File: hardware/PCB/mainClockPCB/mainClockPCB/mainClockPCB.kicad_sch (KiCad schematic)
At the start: 61 parts, among them IC1 TMP275AIDR, IC2 SPX1117M3-L_TR, IC3 MCP7940N-I_P, IC4 PAM8904QJER, J1 USB_C_Receptacle_USB2.0_16P, J2 Conn_01x09_Socket, J3 Conn_01x02_Socket, J4 Conn_01x08, J5 Conn_01x09, J6 Conn_01x09, J7 Conn_01x05, J8 Conn_01x06, J9 Conn_01x05, SW1 SW_Push, SW2 SW_Push, U1 PEC11R-4320K-S0012, U2 USBLC6-2SC6, U3 ESP32-S3-WROOM-2, U4 74HC165, Y1 AB26T-32.768KHZ-6

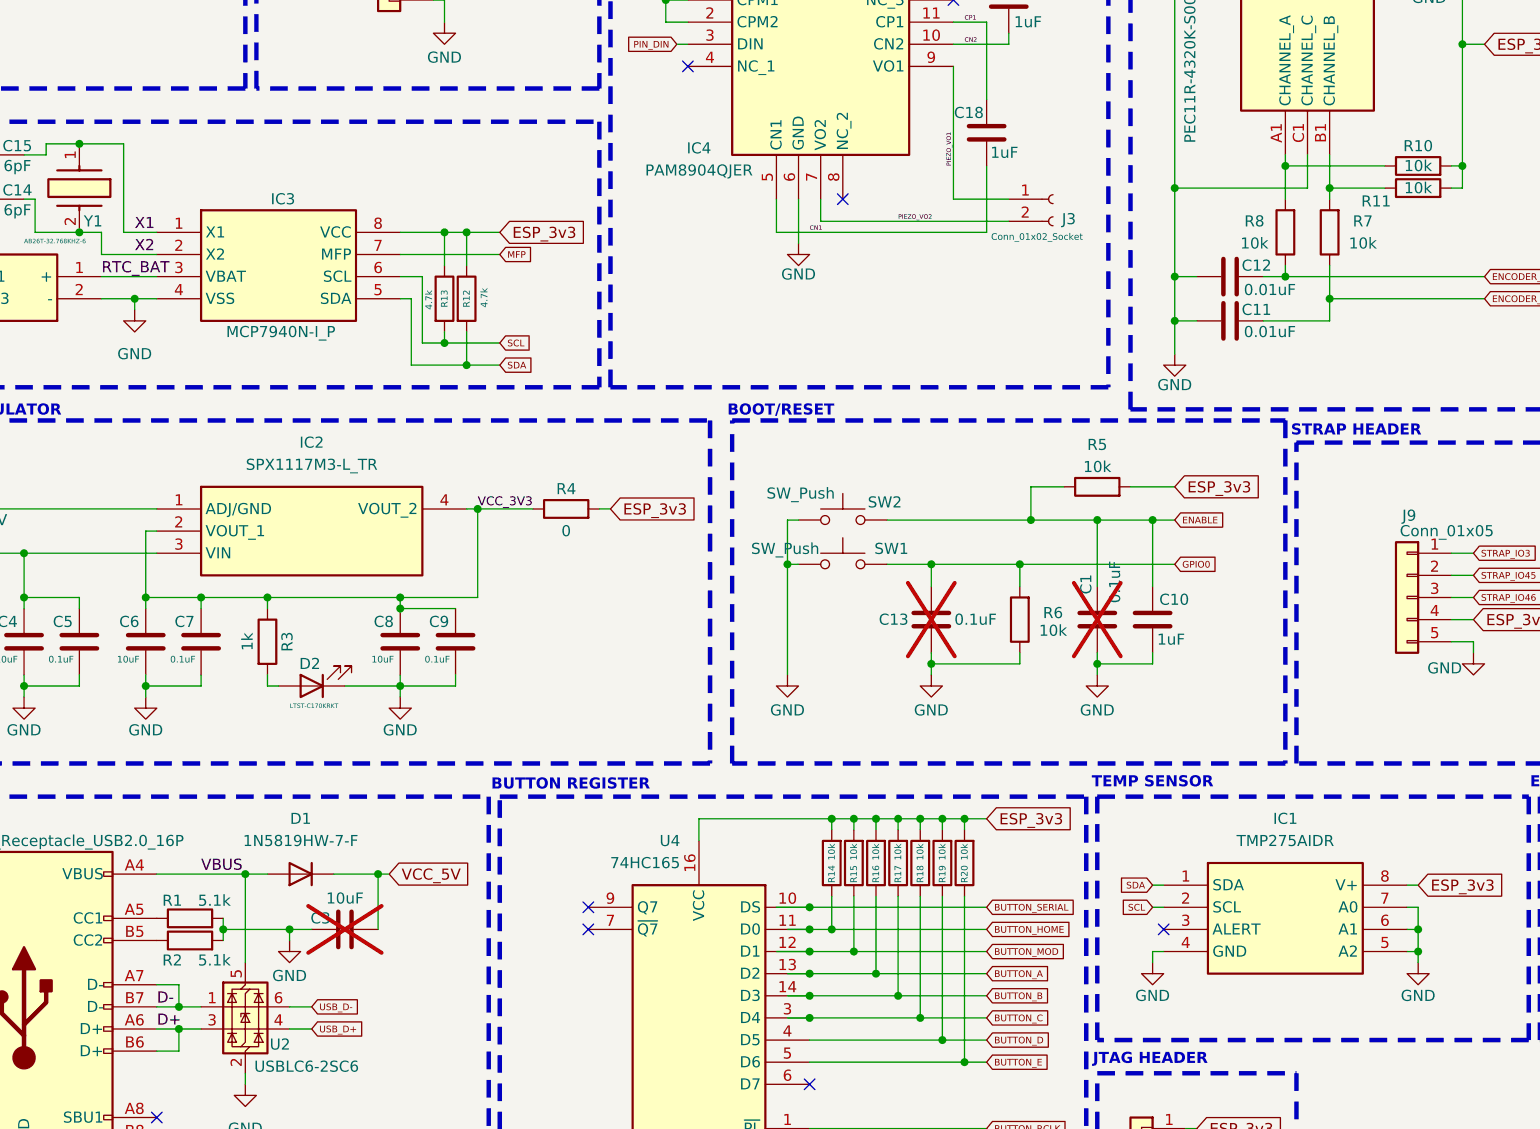
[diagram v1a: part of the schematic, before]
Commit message: net label fixes
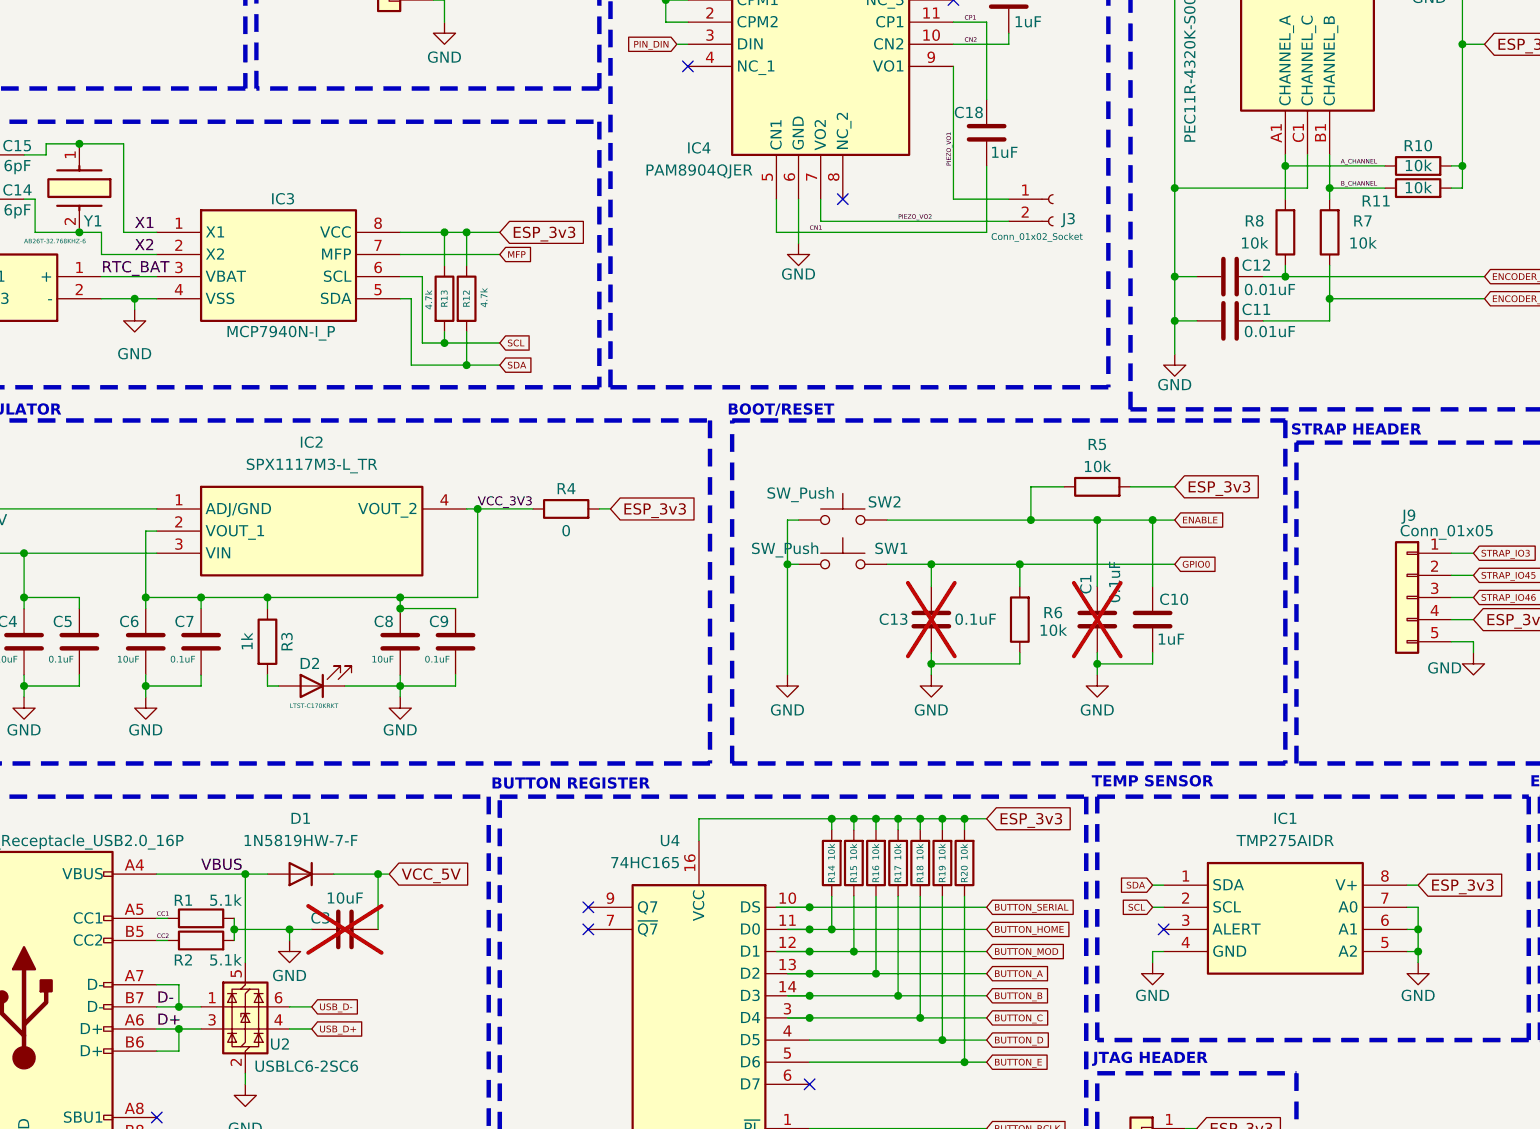
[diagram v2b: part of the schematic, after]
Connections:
- net B_CHANNEL: now reaches R11.1, R7.2, U1.B1 (CHANNEL_B)
- net A_CHANNEL: now reaches R10.1, R8.2, U1.A1 (CHANNEL_A)
- net CC1: now reaches J1.A5 (CC1), R1.1
- net CC2: now reaches J1.B5 (CC2), R2.1
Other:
- moved on the sheet: R1, R2
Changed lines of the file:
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@@
 	)
 	(junction
-		(at 52.07 151.13)
+		(at 53.34 151.13)
 		(diameter 0)
 		(color 0 0 0 0)
@@
 	(wire
 		(pts
-			(xy 52.07 149.86) (xy 52.07 151.13)
+			(xy 53.34 149.86) (xy 53.34 151.13)
 		)
 		(stroke
@@
 	(wire
 		(pts
-			(xy 52.07 151.13) (xy 52.07 152.4)
+			(xy 53.34 151.13) (xy 53.34 152.4)
 		)
 		(stroke
@@
 	(wire
 		(pts
+			(xy 45.72 149.86) (xy 44.45 149.86)
+		)
+		(stroke
+			(width 0)
+			(type default)
+		)
+	)
+	(wire
+		(pts
 			(xy 54.61 144.78) (xy 57.15 144.78)
 		)
@@
 	(wire
 		(pts
-			(xy 52.07 151.13) (xy 59.69 151.13)
+			(xy 53.34 151.13) (xy 59.69 151.13)
 		)
 		(stroke
@@
 	(wire
 		(pts
+			(xy 45.72 152.4) (xy 44.45 152.4)
+		)
+		(stroke
+			(width 0)
+			(type default)
+		)
+	)
+	(wire
+		(pts
 			(xy 134.62 138.43) (xy 134.62 139.7)
 		)
@@
 		)
 	)
+	(label "B_CHANNEL"
+		(at 180.34 66.04 0)
+		(effects
+			(font
+				(size 0.508 0.508)
+			)
+			(justify left bottom)
+		)
+	)
 	(label "X2"
 		(at 41.91 73.66 0)
@@
 		)
 	)
+	(label "A_CHANNEL"
+		(at 180.34 63.5 0)
+		(effects
+			(font
+				(size 0.508 0.508)
+			)
+			(justify left bottom)
+		)
+	)
 	(label "CP1"
 		(at 137.16 46.99 0)
@@
 		)
 	)
+	(label "CC1"
+		(at 44.45 149.86 0)
+		(effects
+			(font
+				(size 0.508 0.508)
+			)
+			(justify left bottom)
+		)
+	)
 	(label "D-"
 		(at 44.45 160.02 0)
@@
 		)
 	)
+	(label "CC2"
+		(at 44.45 152.4 0)
+		(effects
+			(font
+				(size 0.508 0.508)
+			)
+			(justify left bottom)
+		)
+	)
 	(label "VBUS"
 		(at 49.53 144.78 0)
@@
 	(symbol
 		(lib_id "Device:R")
-		(at 48.26 149.86 90)
+		(at 49.53 149.86 90)
 		(unit 1)
 		(exclude_from_sim no)
@@
 		(dnp no)
 		(property "Reference" "R1"
-			(at 46.228 147.828 90)
+			(at 47.498 147.828 90)
 			(effects
 				(font
@@
 		)
 		(property "Value" "5.1k"
-			(at 51.054 147.828 90)
+			(at 52.324 147.828 90)
 			(effects
 				(font
@@
 		)
 		(property "Footprint" "Resistor_SMD:R_0603_1608Metric_Pad0.98x0.95mm_HandSolder"
-			(at 48.26 151.638 90)
+			(at 49.53 151.638 90)
 			(effects
 				(font
@@
 		)
 		(property "Datasheet" "~"
-			(at 48.26 149.86 0)
+			(at 49.53 149.86 0)
 			(effects
 				(font
@@
 		)
 		(property "Description" "Resistor"
-			(at 48.26 149.86 0)
+			(at 49.53 149.86 0)
 			(effects
 				(font
@@
 	(symbol
 		(lib_id "Device:R")
-		(at 48.26 152.4 90)
+		(at 49.53 152.4 90)
 		(unit 1)
 		(exclude_from_sim no)
@@
 		(dnp no)
 		(property "Reference" "R2"
-			(at 46.228 154.686 90)
+			(at 47.498 154.686 90)
 			(effects
 				(font
@@
 		)
 		(property "Value" "5.1k"
-			(at 51.054 154.686 90)
+			(at 52.324 154.686 90)
 			(effects
 				(font
@@
 		)
 		(property "Footprint" "Resistor_SMD:R_0603_1608Metric_Pad0.98x0.95mm_HandSolder"
-			(at 48.26 154.178 90)
+			(at 49.53 154.178 90)
 			(effects
 				(font
@@
 		)
 		(property "Datasheet" "~"
-			(at 48.26 152.4 0)
+			(at 49.53 152.4 0)
 			(effects
 				(font
@@
 		)
 		(property "Description" "Resistor"
-			(at 48.26 152.4 0)
+			(at 49.53 152.4 0)
 			(effects
 				(font

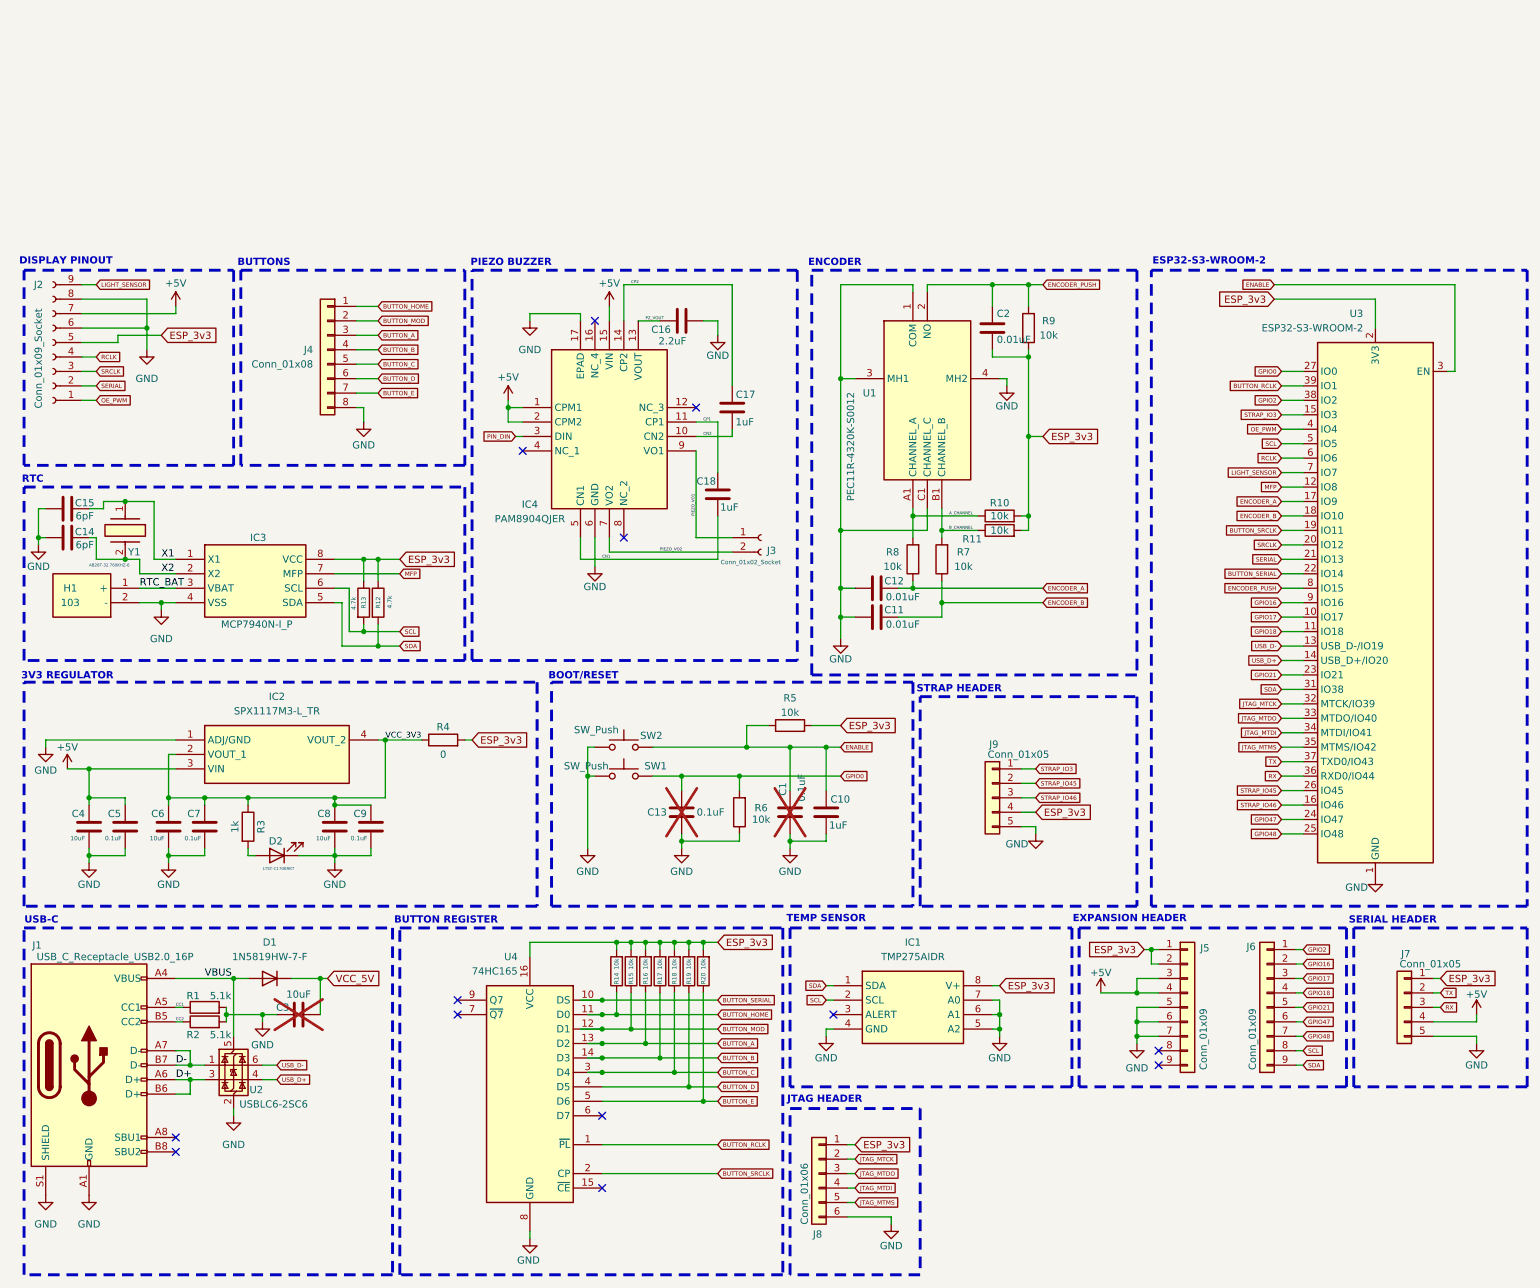
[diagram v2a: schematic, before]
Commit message: power flags
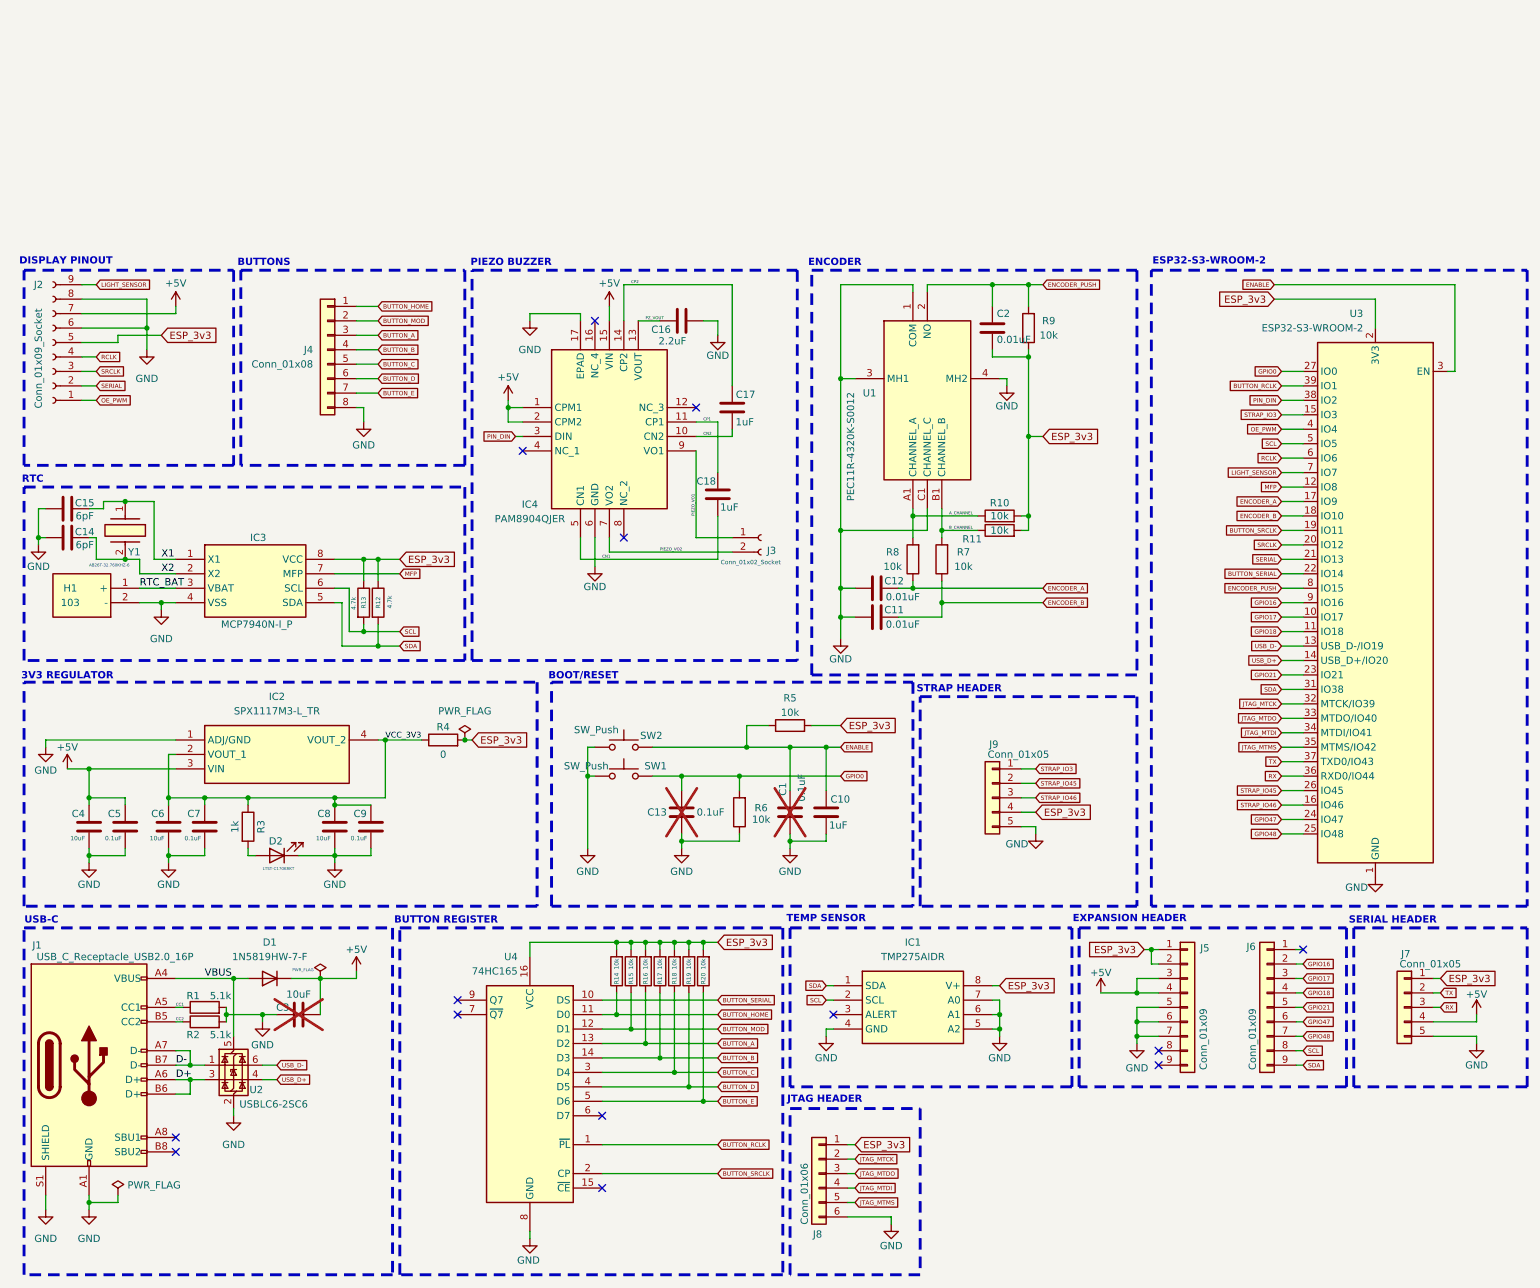
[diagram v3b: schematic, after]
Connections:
- net VCC_5V is gone; now on net +5V: C3.2, D1.1 (K)
- net PIN_DIN: now also U3.38 (IO2)
- net GPIO2: no longer names the net of J6.1 (Pin_1)
- net GPIO2: no longer U3.38 (IO2)
- no-connect marks 13 -> 14

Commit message: PCB design complete
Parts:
- J3: footprint Connector_PinSocket_2.54mm:PinSocket_1x02_P2.54mm_Vertical -> Connector_JST:JST_XH_B2B-XH-A_1x02_P2.50mm_Vertical
- J4: footprint Connector_PinSocket_2.54mm:PinSocket_1x08_P2.54mm_Vertical -> Connector_JST:JST_XH_B8B-XH-A_1x08_P2.50mm_Vertical
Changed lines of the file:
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@@
 			)
 		)
-		(property "Footprint" "Connector_PinSocket_2.54mm:PinSocket_1x08_P2.54mm_Vertical"
+		(property "Footprint" "Connector_JST:JST_XH_B8B-XH-A_1x08_P2.50mm_Vertical"
 			(at 71.12 34.29 0)
 			(effects
@@
 			)
 		)
-		(property "Footprint" "Connector_PinSocket_2.54mm:PinSocket_1x02_P2.54mm_Vertical"
+		(property "Footprint" "Connector_JST:JST_XH_B2B-XH-A_1x02_P2.50mm_Vertical"
 			(at 147.32 67.31 0)
 			(effects

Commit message: initial BOM generation
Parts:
- H1, IC3, J1, J4, J5, J6, J7, J8, SW1, SW2, U1, U4, Y1: now left out of the parts list
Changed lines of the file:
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@@
 		(unit 1)
 		(exclude_from_sim no)
-		(in_bom yes)
+		(in_bom no)
 		(on_board yes)
 		(dnp no)
@@
 		(unit 1)
 		(exclude_from_sim no)
-		(in_bom yes)
+		(in_bom no)
 		(on_board yes)
 		(dnp no)
@@
 		(unit 1)
 		(exclude_from_sim no)
-		(in_bom yes)
+		(in_bom no)
 		(on_board yes)
 		(dnp no)
@@
 		(unit 1)
 		(exclude_from_sim no)
-		(in_bom yes)
+		(in_bom no)
 		(on_board yes)
 		(dnp no)
@@
 		(unit 1)
 		(exclude_from_sim no)
-		(in_bom yes)
+		(in_bom no)
 		(on_board yes)
 		(dnp no)
@@
 		(unit 1)
 		(exclude_from_sim no)
-		(in_bom yes)
+		(in_bom no)
 		(on_board yes)
 		(dnp no)
@@
 		(unit 1)
 		(exclude_from_sim no)
-		(in_bom yes)
+		(in_bom no)
 		(on_board yes)
 		(dnp no)
@@
 		(unit 1)
 		(exclude_from_sim no)
-		(in_bom yes)
+		(in_bom no)
 		(on_board yes)
 		(dnp no)
@@
 		(unit 1)
 		(exclude_from_sim no)
-		(in_bom yes)
+		(in_bom no)
 		(on_board yes)
 		(dnp no)
@@
 		(unit 1)
 		(exclude_from_sim no)
-		(in_bom yes)
+		(in_bom no)
 		(on_board yes)
 		(dnp no)
@@
 		(unit 1)
 		(exclude_from_sim no)
-		(in_bom yes)
+		(in_bom no)
 		(on_board yes)
 		(dnp no)
@@
 		(unit 1)
 		(exclude_from_sim no)
-		(in_bom yes)
+		(in_bom no)
 		(on_board yes)
 		(dnp no)
@@
 		(unit 1)
 		(exclude_from_sim no)
-		(in_bom yes)
+		(in_bom no)
 		(on_board yes)
 		(dnp no)

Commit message: large commit of PCB progress
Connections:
- net GND: now also U4.15 (~{CE})
- no-connect marks 14 -> 13
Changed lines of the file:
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@@
 	)
 	(junction
+		(at 106.68 189.23)
+		(diameter 0)
+		(color 0 0 0 0)
+	)
+	(junction
 		(at 29.21 184.15)
 		(diameter 0)
@@
 	)
 	(no_connect
-		(at 119.38 181.61)
-	)
-	(no_connect
 		(at 93.98 151.13)
 	)
@@
 	(wire
 		(pts
+			(xy 120.65 181.61) (xy 120.65 189.23)
+		)
+		(stroke
+			(width 0)
+			(type default)
+		)
+	)
+	(wire
+		(pts
 			(xy 127 138.43) (xy 127 139.7)
 		)
@@
 	(wire
 		(pts
+			(xy 120.65 189.23) (xy 106.68 189.23)
+		)
+		(stroke
+			(width 0)
+			(type default)
+		)
+	)
+	(wire
+		(pts
 			(xy 161.29 66.04) (xy 176.53 66.04)
 		)
@@
 		)
 		(stroke
+			(width 0)
+			(type default)
+		)
+	)
+	(wire
+		(pts
+			(xy 119.38 181.61) (xy 120.65 181.61)
+		)
+		(stroke
